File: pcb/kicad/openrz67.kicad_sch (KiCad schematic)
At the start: 57 parts, among them J1 GPIO header, U1 ESP32-C3FH4, U2 TPS63031DSKR, U3 BQ25185DLHR, U4 S4B-XH-A(LF)(SN), U5 TLP172AM, U6 TLP172AM, X1 40MHz, X2 32.768kHz

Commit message: PCB: C14/C26/C29 1 µF → Samsung CL10A105KB8NNNC (C15849); HRE part low on stock
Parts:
- C14, C26, C29: symbol openrz67:CGA0603X5R105K500JT -> openrz67:CL10A105KB8NNNC; Manufacturer HRE(芯声) -> Samsung Electro-Mechanics; Manufacturer Part CGA0603X5R105K500JT -> CL10A105KB8NNNC; Supplier Part C6119852 -> C15849
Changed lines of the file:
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@@
     )
   )
-  (symbol (lib_id "openrz67:CGA0603X5R105K500JT") (at 180.34 196.85 90) (unit 1)
+  (symbol (lib_id "openrz67:CL10A105KB8NNNC") (at 180.34 196.85 90) (unit 1)
     (in_bom yes) (on_board yes) (dnp no)
     (property "Reference" "C29" (at 184.15 196.85 90)
@@
       (effects (font (size 1.27 1.27)) hide)
     )
-    (property "Manufacturer Part" "CGA0603X5R105K500JT" (at 180.34 196.85 0)
-      (effects (font (size 1.27 1.27)) hide)
-    )
-    (property "Manufacturer" "HRE(芯声)" (at 180.34 196.85 0)
-      (effects (font (size 1.27 1.27)) hide)
-    )
-    (property "Supplier Part" "C6119852" (at 180.34 196.85 0)
+    (property "Manufacturer Part" "CL10A105KB8NNNC" (at 180.34 196.85 0)
+      (effects (font (size 1.27 1.27)) hide)
+    )
+    (property "Manufacturer" "Samsung Electro-Mechanics" (at 180.34 196.85 0)
+      (effects (font (size 1.27 1.27)) hide)
+    )
+    (property "Supplier Part" "C15849" (at 180.34 196.85 0)
       (effects (font (size 1.27 1.27)) hide)
     )
@@
     )
   )
-  (symbol (lib_id "openrz67:CGA0603X5R105K500JT") (at 354.33 40.64 90) (unit 1)
+  (symbol (lib_id "openrz67:CL10A105KB8NNNC") (at 354.33 40.64 90) (unit 1)
     (in_bom yes) (on_board yes) (dnp no)
     (property "Reference" "C26" (at 358.14 40.64 90)
@@
       (effects (font (size 1.27 1.27)) hide)
     )
-    (property "Manufacturer Part" "CGA0603X5R105K500JT" (at 354.33 40.64 0)
-      (effects (font (size 1.27 1.27)) hide)
-    )
-    (property "Manufacturer" "HRE(芯声)" (at 354.33 40.64 0)
-      (effects (font (size 1.27 1.27)) hide)
-    )
-    (property "Supplier Part" "C6119852" (at 354.33 40.64 0)
+    (property "Manufacturer Part" "CL10A105KB8NNNC" (at 354.33 40.64 0)
+      (effects (font (size 1.27 1.27)) hide)
+    )
+    (property "Manufacturer" "Samsung Electro-Mechanics" (at 354.33 40.64 0)
+      (effects (font (size 1.27 1.27)) hide)
+    )
+    (property "Supplier Part" "C15849" (at 354.33 40.64 0)
       (effects (font (size 1.27 1.27)) hide)
     )
@@
     )
   )
-  (symbol (lib_id "openrz67:CGA0603X5R105K500JT") (at 100.33 205.74 90) (unit 1)
+  (symbol (lib_id "openrz67:CL10A105KB8NNNC") (at 100.33 205.74 90) (unit 1)
     (in_bom yes) (on_board yes) (dnp no)
     (property "Reference" "C14" (at 104.14 205.74 90)
@@
       (effects (font (size 1.27 1.27)) hide)
     )
-    (property "Manufacturer Part" "CGA0603X5R105K500JT" (at 100.33 205.74 0)
-      (effects (font (size 1.27 1.27)) hide)
-    )
-    (property "Manufacturer" "HRE(芯声)" (at 100.33 205.74 0)
-      (effects (font (size 1.27 1.27)) hide)
-    )
-    (property "Supplier Part" "C6119852" (at 100.33 205.74 0)
-      (effects (font (size 1.27 1.27)) hide)
-    )
+    (property "Manufacturer Part" "CL10A105KB8NNNC" (at 100.33 205.74 0)
+      (effects (font (size 1.27 1.27)) hide)
+    )
+    (property "Manufacturer" "Samsung Electro-Mechanics" (at 100.33 205.74 0)
+      (effects (font (size 1.27 1.27)) hide)
+    )
+    (property "Supplier Part" "C15849" (at 100.33 205.74 0)
+      (effects (font (size 1.27 1.27)) hide)
+    )

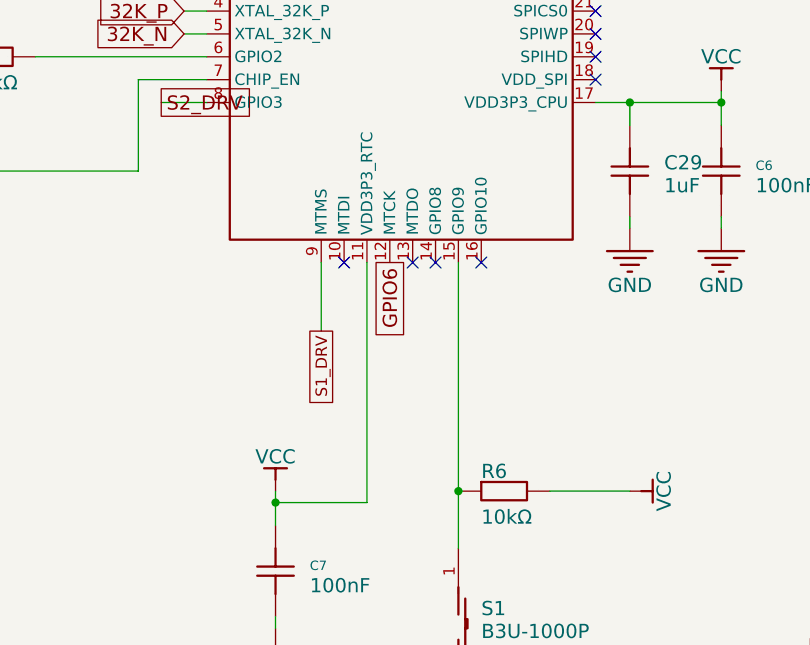
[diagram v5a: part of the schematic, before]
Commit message: PCB: R23 10k pull-up on GPIO8 (strapping pin was floating); C29 +0.55 mm, GPIO6 via moved, VCC artery on x 25.709
GPIO8 needs to be high for Joint Download Boot and has no internal pull;
rev 1 and the ordered rev 2 leave it floating behind a no-connect flag.
Also adds the 2026-09-10 design review and its adversarial counter-read
under notes/. VDD_SPI 1 uF not added: no room on the top side (README).
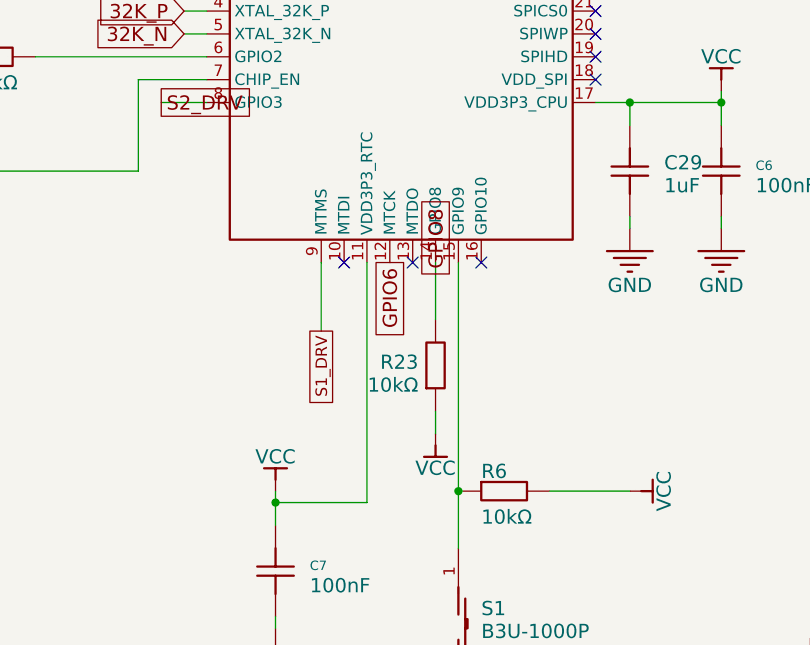
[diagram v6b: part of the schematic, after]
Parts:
- added R23: 10kΩ, openrz67:R0402, symbol openrz67:0402WGF1002TCE
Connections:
- net VCC: now also R23.1
- net GPIO8: now reaches U1.14 (GPIO8)
- net GPIO8: now also R23.2
- no-connect marks 15 -> 14
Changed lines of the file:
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@@
   (no_connect (at 163.83 207.01))
   (no_connect (at 176.53 179.07))
-  (no_connect (at 158.75 207.01))
   (no_connect (at 212.09 274.32))
   (no_connect (at 176.51 34.19))
+  (wire (pts (xy 158.75 207.01) (xy 158.75 213.36))
+    (stroke (width 0) (type default))
+  )
+  (wire (pts (xy 158.75 223.52) (xy 158.75 226.06))
+    (stroke (width 0) (type default))
+  )
   (wire (pts (xy 146.05 153.67) (xy 146.05 140.97))
     (stroke (width 0) (type default))
@@
   )
   (text "S1_DRV = GPIO4, S2_DRV = GPIO3 (src/main.cpp)" (at 245.11 170.18 0)
+    (effects (font (size 1.5748 1.5748)) (justify left bottom))
+  )
+  (global_label "GPIO8" (shape passive) (at 158.75 208.28 90)
     (effects (font (size 1.5748 1.5748)) (justify left bottom))
   )
@@
         )
       )
+    )
+  )
+  (symbol (lib_id "openrz67:0402WGF1002TCE") (at 158.75 218.44 90) (unit 1)
+    (in_bom yes) (on_board yes) (dnp no)
+    (property "Reference" "R23" (at 156.845 217.17 90)
+      (effects (font (size 1.5748 1.5748)) (justify left bottom))
+    )
+    (property "Value" "10kΩ" (at 156.845 219.71 90)
+      (effects (font (size 1.5748 1.5748)) (justify left bottom))
+    )
+    (property "Footprint" "openrz67:R0402" (at 158.75 218.44 0)
+      (effects (font (size 1.27 1.27)) hide)
+    )
+    (property "Datasheet" "https://www.lcsc.com/product-detail/C25744.html" (at 158.75 218.44 0)
+      (effects (font (size 1.27 1.27)) hide)
+    )
+    (property "Description" "" (at 158.75 218.44 0)
+      (effects (font (size 1.27 1.27)) hide)
+    )
+    (property "Manufacturer Part" "0402WGF1002TCE" (at 158.75 218.44 0)
+      (effects (font (size 1.27 1.27)) hide)
+    )
+    (property "Manufacturer" "UNI-ROYAL(厚声)" (at 158.75 218.44 0)
+      (effects (font (size 1.27 1.27)) hide)
+    )
+    (property "Supplier Part" "C25744" (at 158.75 218.44 0)
+      (effects (font (size 1.27 1.27)) hide)
+    )
+    (property "Supplier" "LCSC" (at 158.75 218.44 0)
+      (effects (font (size 1.27 1.27)) hide)
+    )
+    (property "LCSC Part Name" "10kΩ ±1% 62.5mW 厚膜电阻" (at 158.75 218.44 0)
+      (effects (font (size 1.27 1.27)) hide)
+    )
+    (pin "1")
+    (pin "2")
+    (instances
+      (project "openrz67"
+        (path "/608428cc-ede5-4359-a9e7-0ca7713b40fb"
+          (reference "R23") (unit 1)
+        )
+      )
+    )
+  )
+  (symbol (lib_id "openrz67:Power-VCC") (at 158.75 226.06 180) (unit 1)
+    (in_bom yes) (on_board yes) (dnp no)
+    (property "Reference" "#PWR065" (at 158.75 226.06 0)
+      (effects (font (size 1.27 1.27)) hide)
+    )
+    (property "Value" "VCC" (at 158.75 229.87 0)
+      (effects (font (size 1.5748 1.5748)))
+    )
+    (property "Footprint" "" (at 158.75 226.06 0)
+      (effects (font (size 1.27 1.27)) hide)
+    )
+    (property "Datasheet" "" (at 158.75 226.06 0)
+      (effects (font (size 1.27 1.27)) hide)
+    )
+    (property "Description" "" (at 158.75 226.06 0)
+      (effects (font (size 1.27 1.27)) hide)
+    )
+    (pin "1")
+    (instances
+      (project "openrz67"
+        (path "/608428cc-ede5-4359-a9e7-0ca7713b40fb"
+          (reference "#PWR065") (unit 1)
+        )
+      )
